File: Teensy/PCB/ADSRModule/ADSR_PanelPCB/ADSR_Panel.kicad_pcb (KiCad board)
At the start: 2 copper layers, 58.4 x 128 mm, 21 parts, among them SW1 Mode_Switch

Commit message: Generated Gerbers
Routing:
- added copper zone on B.Cu, net shielding
- added copper zone on F.Cu, net shielding
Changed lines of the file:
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@@
     (pad_to_mask_clearance 0)
     (pcbplotparams
-      (layerselection 0x0080000_7ffffffe)
+      (layerselection 0x00010fc_ffffffff)
       (disableapertmacros false)
-      (usegerberextensions false)
-      (usegerberattributes true)
-      (usegerberadvancedattributes true)
-      (creategerberjobfile true)
+      (usegerberextensions true)
+      (usegerberattributes false)
+      (usegerberadvancedattributes false)
+      (creategerberjobfile false)
       (svguseinch false)
       (svgprecision 6)
-      (excludeedgelayer false)
+      (excludeedgelayer true)
       (plotframeref false)
       (viasonmask false)
@@
       (psa4output false)
       (plotreference true)
-      (plotvalue true)
+      (plotvalue false)
       (plotinvisibletext false)
       (sketchpadsonfab false)
-      (subtractmaskfromsilk false)
-      (outputformat 5)
+      (subtractmaskfromsilk true)
+      (outputformat 1)
       (mirror false)
       (drillshape 0)
       (scaleselection 1)
-      (outputdirectory "")
+      (outputdirectory "ADSR_Panel_Gerber/")
     )
   )
   (net 0 "")
+  (net 1 "shielding")
   (footprint "Potentiometer:Bourns_PTV09A-X_Hole" (layer "F.Cu")
     (at 129.54 109.22)
@@
       (effects (font (size 1 1) (thickness 0.15)))
     )
-    (fp_line (start -2.54 -64) (end 2.54 -64) (layer "User.1") (width 0.12))
     (fp_line (start -2.54 64) (end 2.54 64) (layer "User.1") (width 0.12))
+    (fp_line (start -2.54 -64) (end 2.54 -64) (layer "User.1") (width 0.12))
     (fp_circle (center 0 0) (end 0 0) (layer "User.1") (width 0.12) (fill none))
-    (fp_line (start -1.27 -62.85) (end 1.27 -62.85) (layer "User.2") (width 0.12))
-    (fp_line (start -1.27 -59.65) (end 1.27 -59.65) (layer "User.2") (width 0.12))
-    (fp_line (start -1.27 59.65) (end 1.27 59.65) (layer "User.2") (width 0.12))
-    (fp_line (start -1.27 62.85) (end 1.27 62.85) (layer "User.2") (width 0.12))
-    (fp_arc (start 1.27 59.65) (mid 2.87 61.25) (end 1.27 62.85) (layer "User.2") (width 0.12))
-    (fp_arc (start -1.27 62.85) (mid -2.87 61.25) (end -1.27 59.65) (layer "User.2") (width 0.12))
-    (fp_arc (start 1.27 -62.85) (mid 2.87 -61.25) (end 1.27 -59.65) (layer "User.2") (width 0.12))
-    (fp_arc (start -1.27 -59.65) (mid -2.87 -61.25) (end -1.27 -62.85) (layer "User.2") (width 0.12))
-    (pad "" np_thru_hole oval (at 0 -61.25) (size 5.74 3.2) (drill oval 5.74 3.2) (layers *.Mask))
-    (pad "" np_thru_hole oval (at 0 61.25) (size 5.74 3.2) (drill oval 5.74 3.2) (layers *.Mask))
+    (fp_line (start -1.6 62.85) (end 1.6 62.85) (layer "User.2") (width 0.12))
+    (fp_line (start -1.6 -59.65) (end 1.6 -59.65) (layer "User.2") (width 0.12))
+    (fp_line (start -1.6 -62.85) (end 1.6 -62.85) (layer "User.2") (width 0.12))
+    (fp_line (start -1.6 59.65) (end 1.6 59.65) (layer "User.2") (width 0.12))
+    (fp_arc (start 1.6 59.65) (mid 3.2 61.25) (end 1.6 62.85) (layer "User.2") (width 0.12))
+    (fp_arc (start 1.6 -62.85) (mid 3.2 -61.25) (end 1.6 -59.65) (layer "User.2") (width 0.12))
+    (fp_arc (start -1.6 62.85) (mid -3.2 61.25) (end -1.6 59.65) (layer "User.2") (width 0.12))
+    (fp_arc (start -1.6 -59.65) (mid -3.2 -61.25) (end -1.6 -62.85) (layer "User.2") (width 0.12))
+    (pad "1" thru_hole oval (at 0 61.25) (size 7.4 4.2) (drill oval 6.4 3.2) (layers *.Cu *.Mask)
+      (net 1 "shielding"))
+    (pad "1" thru_hole oval (at 0 -61.25) (size 7.4 4.2) (drill oval 6.4 3.2) (layers *.Cu *.Mask)
+      (net 1 "shielding"))
   )
   (footprint "Potentiometer:Bourns_PTV09A-X_Hole" (layer "F.Cu")
@@
     (fp_line (start -2.54 -64) (end 2.54 -64) (layer "User.1") (width 0.12))
     (fp_circle (center 0 0) (end 0 0) (layer "User.1") (width 0.12) (fill none))
-    (fp_line (start -1.27 -62.85) (end 1.27 -62.85) (layer "User.2") (width 0.12))
-    (fp_line (start -1.27 -59.65) (end 1.27 -59.65) (layer "User.2") (width 0.12))
-    (fp_line (start -1.27 59.65) (end 1.27 59.65) (layer "User.2") (width 0.12))
-    (fp_line (start -1.27 62.85) (end 1.27 62.85) (layer "User.2") (width 0.12))
-    (fp_arc (start 1.27 59.65) (mid 2.87 61.25) (end 1.27 62.85) (layer "User.2") (width 0.12))
-    (fp_arc (start -1.27 62.85) (mid -2.87 61.25) (end -1.27 59.65) (layer "User.2") (width 0.12))
-    (fp_arc (start -1.27 -59.65) (mid -2.87 -61.25) (end -1.27 -62.85) (layer "User.2") (width 0.12))
-    (fp_arc (start 1.27 -62.85) (mid 2.87 -61.25) (end 1.27 -59.65) (layer "User.2") (width 0.12))
-    (pad "" np_thru_hole oval (at 0 61.25) (size 5.74 3.2) (drill oval 5.74 3.2) (layers *.Mask))
-    (pad "" np_thru_hole oval (at 0 -61.25) (size 5.74 3.2) (drill oval 5.74 3.2) (layers *.Mask))
+    (fp_line (start -1.6 -62.85) (end 1.6 -62.85) (layer "User.2") (width 0.12))
+    (fp_line (start -1.6 59.65) (end 1.6 59.65) (layer "User.2") (width 0.12))
+    (fp_line (start -1.6 62.85) (end 1.6 62.85) (layer "User.2") (width 0.12))
+    (fp_line (start -1.6 -59.65) (end 1.6 -59.65) (layer "User.2") (width 0.12))
+    (fp_arc (start -1.6 62.85) (mid -3.2 61.25) (end -1.6 59.65) (layer "User.2") (width 0.12))
+    (fp_arc (start 1.6 -62.85) (mid 3.2 -61.25) (end 1.6 -59.65) (layer "User.2") (width 0.12))
+    (fp_arc (start 1.6 59.65) (mid 3.2 61.25) (end 1.6 62.85) (layer "User.2") (width 0.12))
+    (fp_arc (start -1.6 -59.65) (mid -3.2 -61.25) (end -1.6 -62.85) (layer "User.2") (width 0.12))
+    (pad "1" thru_hole oval (at 0 61.25) (size 7.4 4.2) (drill oval 6.4 3.2) (layers *.Cu *.Mask)
+      (net 1 "shielding"))
+    (pad "1" thru_hole oval (at 0 -61.25) (size 7.4 4.2) (drill oval 6.4 3.2) (layers *.Cu *.Mask)
+      (net 1 "shielding"))
   )
   (footprint "Perfboard:3.5mm Jack Perfboard_Hole" (layer "F.Cu")
@@
   (gr_rect (start 101.6 47.76) (end 160.02 175.76) (layer "Edge.Cuts") (width 0.1) (fill none))
   (gr_rect (start 104.14 165.1) (end 157.48 58.42) (layer "User.2") (width 0.15) (fill none))
+  (zone (net 1) (net_name "shielding") (layers F&B.Cu) (hatch edge 0.508)
+    (connect_pads yes (clearance 0.508))
+    (min_thickness 0.254) (filled_areas_thickness no)
+    (fill yes (thermal_gap 0.508) (thermal_bridge_width 0.508))
+    (polygon
+      (pts
+        (xy 160.02 175.768)
+        (xy 101.6 175.768)
+        (xy 101.6 47.752)
+        (xy 160.02 47.752)
+      )
+    )
+  )
 )

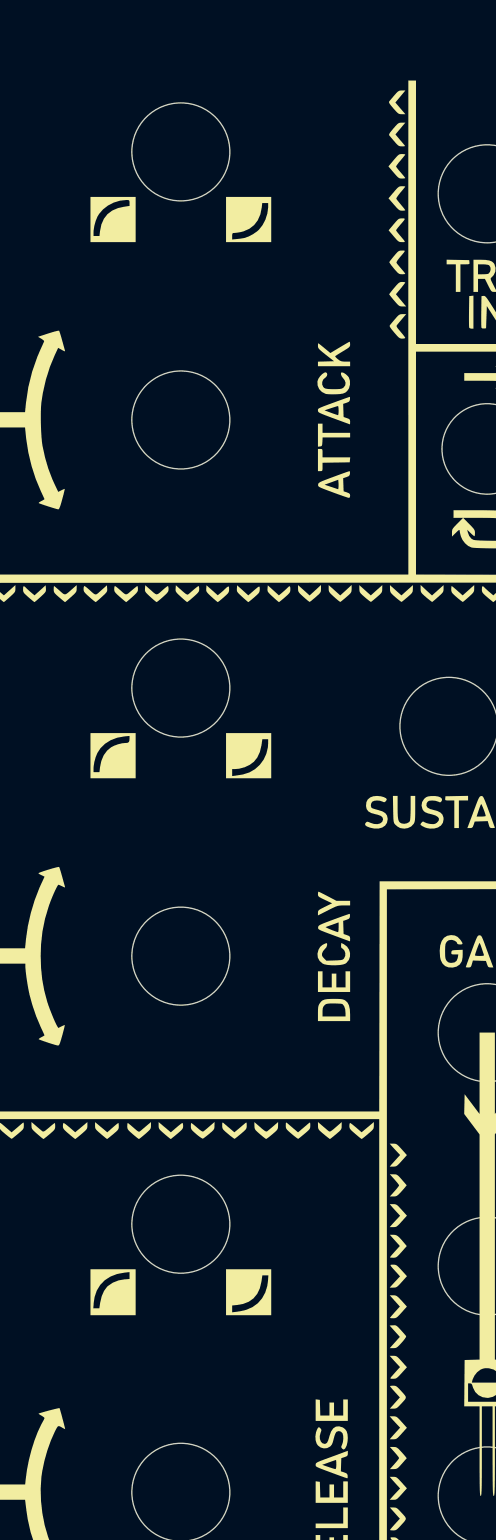
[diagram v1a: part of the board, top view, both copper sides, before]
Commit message: Made NPTH holes 0.5mm bigger; adjusted diode pads for better solderability
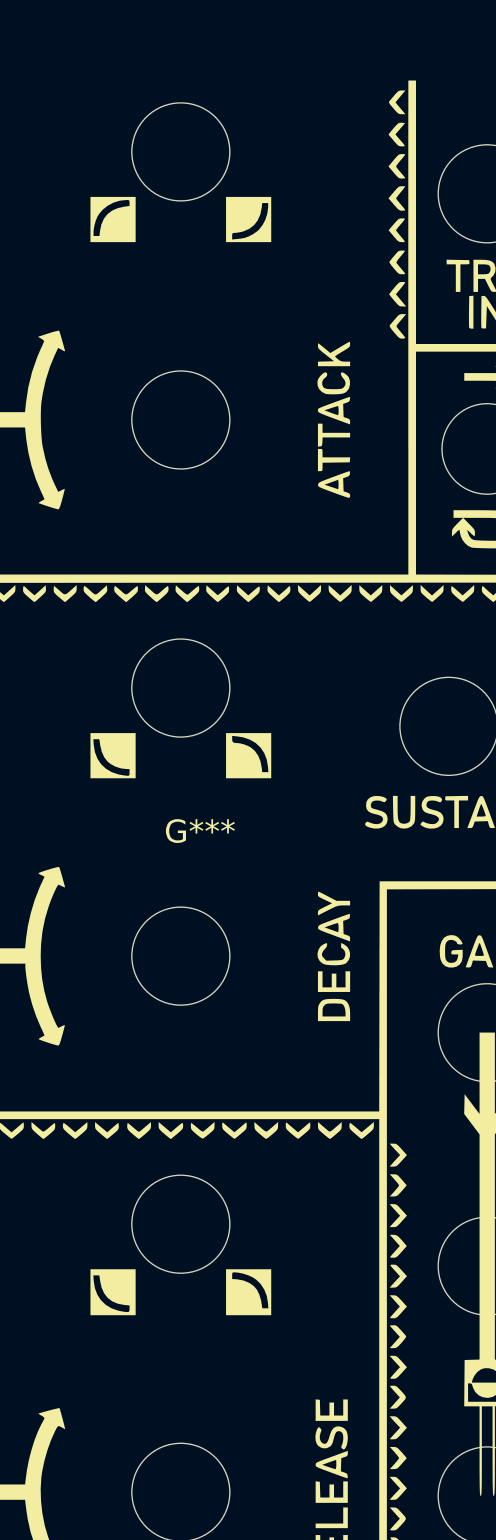
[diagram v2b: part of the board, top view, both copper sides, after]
